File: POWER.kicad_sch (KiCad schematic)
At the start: 26 parts, among them IC1 ECP5-BGA256, U1 AP3429-A, U2 TPS74625, U3 AP3429-A, U4 TPS74611

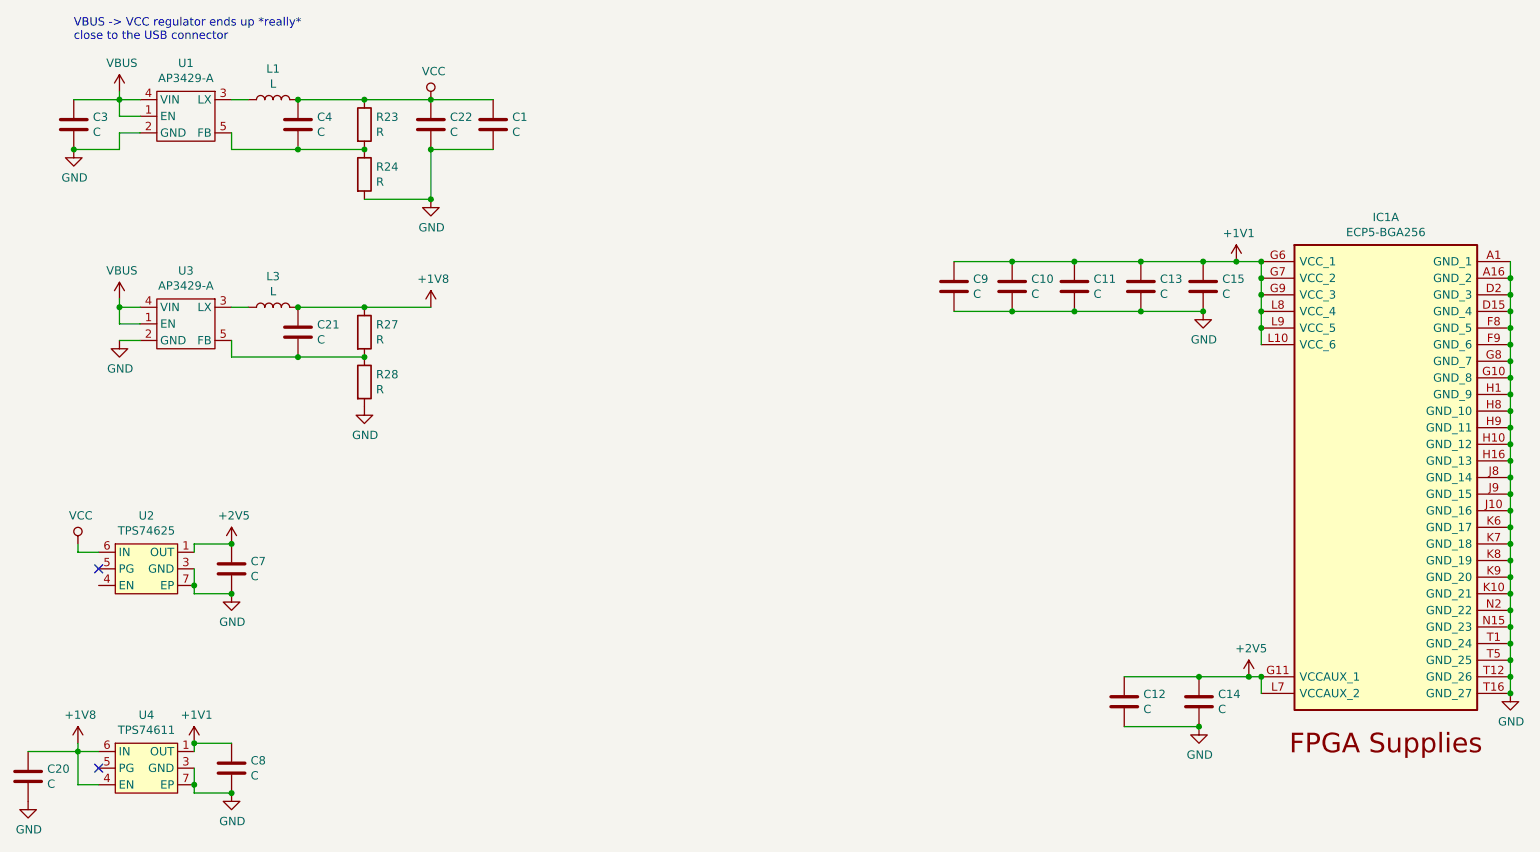
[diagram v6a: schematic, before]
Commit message: Remove SD card, relocate regulators
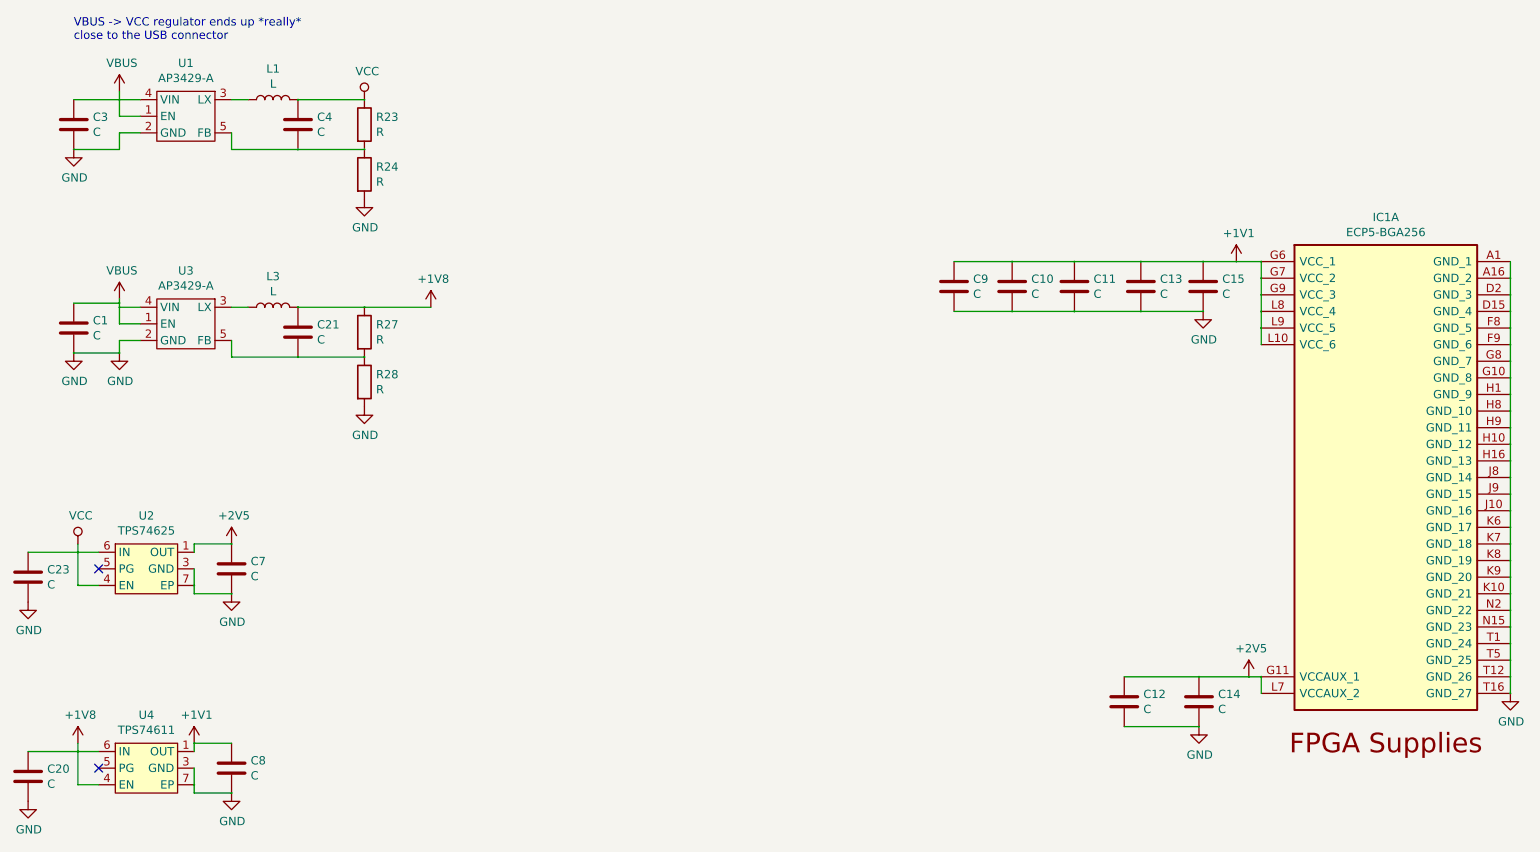
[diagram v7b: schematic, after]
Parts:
- removed C22: C, Capacitor_SMD:C_0402_1005Metric, symbol Device:C
- added C23: C, Capacitor_SMD:C_0805_2012Metric, symbol Device:C
- C1: footprint Capacitor_SMD:C_0402_1005Metric -> Capacitor_SMD:C_0805_2012Metric
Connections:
- net GND: now also C23.2
- net VBUS: now also C1.1
- net VCC: now also U2.4 (EN), C23.1; no longer C1.1
